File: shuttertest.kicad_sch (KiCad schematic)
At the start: 16 parts, among them J1 Conn_01x20_Female, J2 Conn_01x06_Male, J5 Conn_01x06_Male, SW1 SW_Push, U1 ATmega328PB-A, Y1 8M

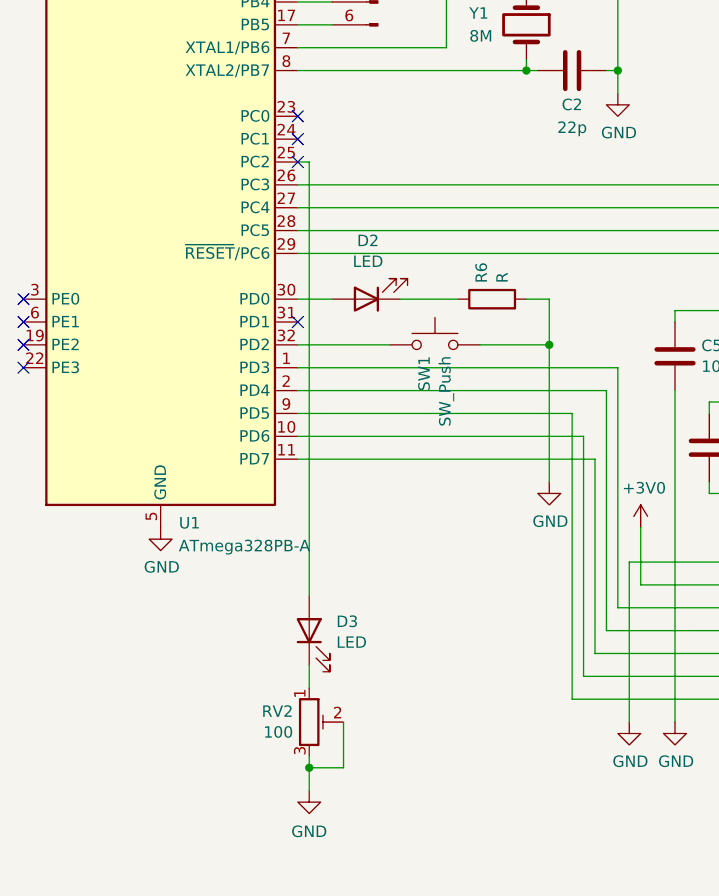
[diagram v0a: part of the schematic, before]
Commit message: Add fixed series resistor to backight trimpot
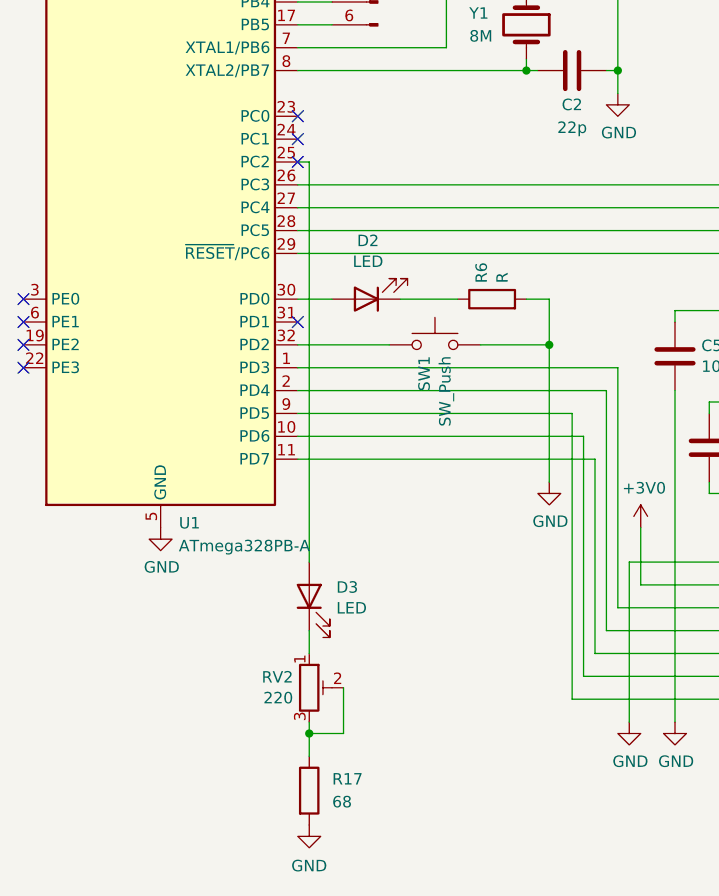
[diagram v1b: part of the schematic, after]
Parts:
- added R17: 68, Resistor_SMD:R_0805_2012Metric_Pad1.20x1.40mm_HandSolder, symbol Device:R
- RV2: value 100 -> 220
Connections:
- net GND: now also R17.2; no longer RV2.2, RV2.3
- new net: R17.1, RV2.2, RV2.3
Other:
- moved on the sheet: D3, RV2
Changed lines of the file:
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@@
 	)
 	(junction
-		(at 66.04 184.15)
+		(at 66.04 180.34)
 		(diameter 0)
 		(color 0 0 0 0)
@@
 	(wire
 		(pts
-			(xy 66.04 172.72) (xy 66.04 175.26)
+			(xy 66.04 168.91) (xy 66.04 171.45)
 		)
 		(stroke
@@
 	(wire
 		(pts
-			(xy 66.04 116.84) (xy 66.04 165.1)
-		)
-		(stroke
-			(width 0)
-			(type default)
-		)
-	)
-	(wire
-		(pts
 			(xy 106.68 133.35) (xy 116.84 133.35)
 		)
@@
 	(wire
 		(pts
-			(xy 69.85 184.15) (xy 66.04 184.15)
+			(xy 69.85 180.34) (xy 66.04 180.34)
 		)
 		(stroke
@@
 	(wire
 		(pts
-			(xy 66.04 184.15) (xy 66.04 186.69)
+			(xy 66.04 180.34) (xy 66.04 182.88)
 		)
 		(stroke
@@
 	(wire
 		(pts
-			(xy 66.04 182.88) (xy 66.04 184.15)
+			(xy 66.04 179.07) (xy 66.04 180.34)
 		)
 		(stroke
@@
 	(wire
 		(pts
-			(xy 69.85 179.07) (xy 69.85 184.15)
+			(xy 69.85 175.26) (xy 69.85 180.34)
 		)
 		(stroke
@@
 		(pts
 			(xy 130.81 129.54) (xy 130.81 130.81)
+		)
+		(stroke
+			(width 0)
+			(type default)
+		)
+	)
+	(wire
+		(pts
+			(xy 66.04 116.84) (xy 66.04 161.29)
 		)
 		(stroke
@@
 	(symbol
 		(lib_id "Device:LED")
-		(at 66.04 168.91 90)
+		(at 66.04 165.1 90)
 		(unit 1)
 		(exclude_from_sim no)
@@
 		(dnp no)
 		(property "Reference" "D3"
-			(at 69.0372 167.9194 90)
+			(at 69.0372 164.1094 90)
 			(effects
 				(font
@@
 		)
 		(property "Value" "LED"
-			(at 69.0372 170.2308 90)
+			(at 69.0372 166.4208 90)
 			(effects
 				(font
@@
 		)
 		(property "Footprint" "display:DEM_128064N"
-			(at 66.04 168.91 0)
+			(at 66.04 165.1 0)
 			(effects
 				(font
@@
 		)
 		(property "Datasheet" "~"
-			(at 66.04 168.91 0)
+			(at 66.04 165.1 0)
 			(effects
 				(font
@@
 		)
 		(property "Description" ""
-			(at 66.04 168.91 0)
+			(at 66.04 165.1 0)
 			(effects
 				(font
@@
 	(symbol
 		(lib_id "Device:R_POT_TRIM")
-		(at 66.04 179.07 0)
+		(at 66.04 175.26 0)
 		(unit 1)
 		(exclude_from_sim no)
@@
 		(dnp no)
 		(property "Reference" "RV2"
-			(at 64.262 177.9016 0)
+			(at 64.262 174.0916 0)
 			(effects
 				(font
@@
 			)
 		)
-		(property "Value" "100"
-			(at 64.262 180.213 0)
+		(property "Value" "220"
+			(at 64.262 176.403 0)
 			(effects
 				(font
@@
 		)
 		(property "Footprint" "Potentiometer_SMD:Potentiometer_Vishay_TS53YL_Vertical"
-			(at 66.04 179.07 0)
+			(at 66.04 175.26 0)
 			(effects
 				(font
@@
 		)
 		(property "Datasheet" "~"
-			(at 66.04 179.07 0)
+			(at 66.04 175.26 0)
 			(effects
 				(font
@@
 		)
 		(property "Description" ""
-			(at 66.04 179.07 0)
+			(at 66.04 175.26 0)
 			(effects
 				(font
@@
 	)
 	(symbol
+		(lib_id "Device:R")
+		(at 66.04 186.69 0)
+		(unit 1)
+		(exclude_from_sim no)
+		(in_bom yes)
+		(on_board yes)
+		(dnp no)
+		(fields_autoplaced yes)
+		(property "Reference" "R17"
+			(at 68.58 185.4199 0)
+			(effects
+				(font
+					(size 1.27 1.27)
+				)
+				(justify left)
+			)
+		)
+		(property "Value" "68"
+			(at 68.58 187.9599 0)
+			(effects
+				(font
+					(size 1.27 1.27)
+				)
+				(justify left)
+			)
+		)
+		(property "Footprint" "Resistor_SMD:R_0805_2012Metric_Pad1.20x1.40mm_HandSolder"
+			(at 64.262 186.69 90)
+			(effects
+				(font
+					(size 1.27 1.27)
+				)
+				(hide yes)
+			)
+		)
+		(property "Datasheet" "~"
+			(at 66.04 186.69 0)
+			(effects
+				(font
+					(size 1.27 1.27)
+				)
+				(hide yes)
+			)
+		)
+		(property "Description" "Resistor"
+			(at 66.04 186.69 0)
+			(effects
+				(font
+					(size 1.27 1.27)
+				)
+				(hide yes)
+			)
+		)
+		(pin "1"
+		)
+		(pin "2"
+		)
+		(instances
+			(project ""
+				(path "/e8c50f1b-c316-4110-9cce-5c24c65a1eaa"
+					(reference "R17")
+					(unit 1)
+				)
+			)
+		)
+	)
+	(symbol
 		(lib_id "MCU_Microchip_ATmega:ATmega328PB-A")
 		(at 49.53 119.38 0)
@@
 	(symbol
 		(lib_id "power:GND")
-		(at 66.04 186.69 0)
+		(at 66.04 190.5 0)
 		(unit 1)
 		(exclude_from_sim no)
@@
 		(fields_autoplaced yes)
 		(property "Reference" "#PWR012"
-			(at 66.04 193.04 0)
+			(at 66.04 196.85 0)
 			(effects
 				(font
@@
 		)
 		(property "Value" "GND"
-			(at 66.04 191.2525 0)
+			(at 66.04 195.0625 0)
 			(effects
 				(font
@@
 		)
 		(property "Footprint" ""
-			(at 66.04 186.69 0)
+			(at 66.04 190.5 0)
 			(effects
 				(font
@@
 		)
 		(property "Datasheet" ""
-			(at 66.04 186.69 0)
+			(at 66.04 190.5 0)
 			(effects
 				(font
@@
 		)
 		(property "Description" ""
-			(at 66.04 186.69 0)
-			(effects
-				(font
+			(at 66.04 190.5 0)
+			(effects
+				(font
